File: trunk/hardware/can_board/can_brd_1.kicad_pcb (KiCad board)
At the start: 2 copper layers, 33.5 x 10.9 mm, 9 parts, among them P1 CONN_4, P2 CONN_2, U1 MCP2551

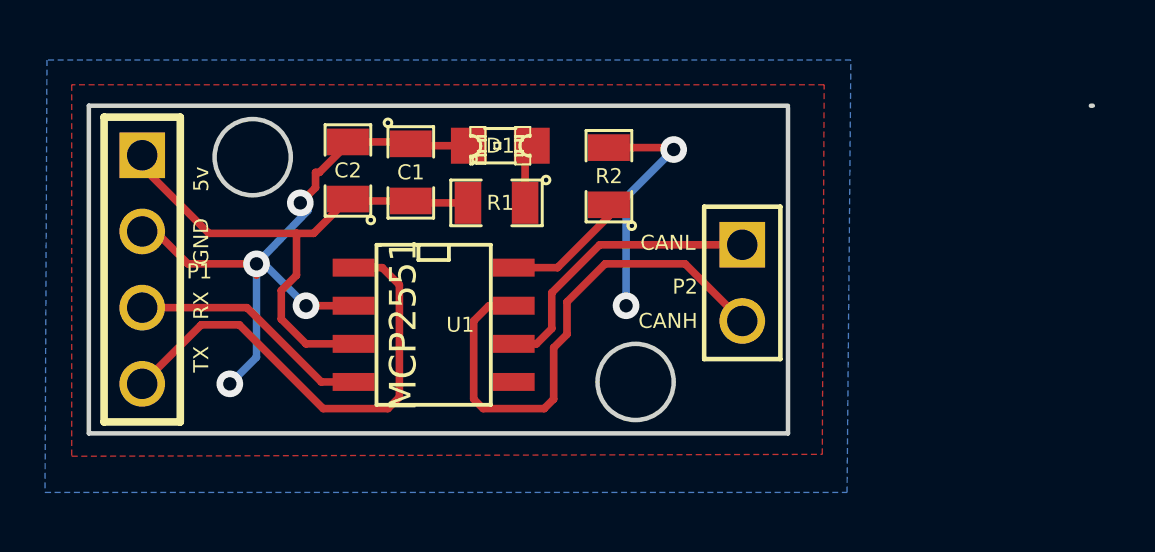
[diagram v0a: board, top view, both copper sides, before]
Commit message: 
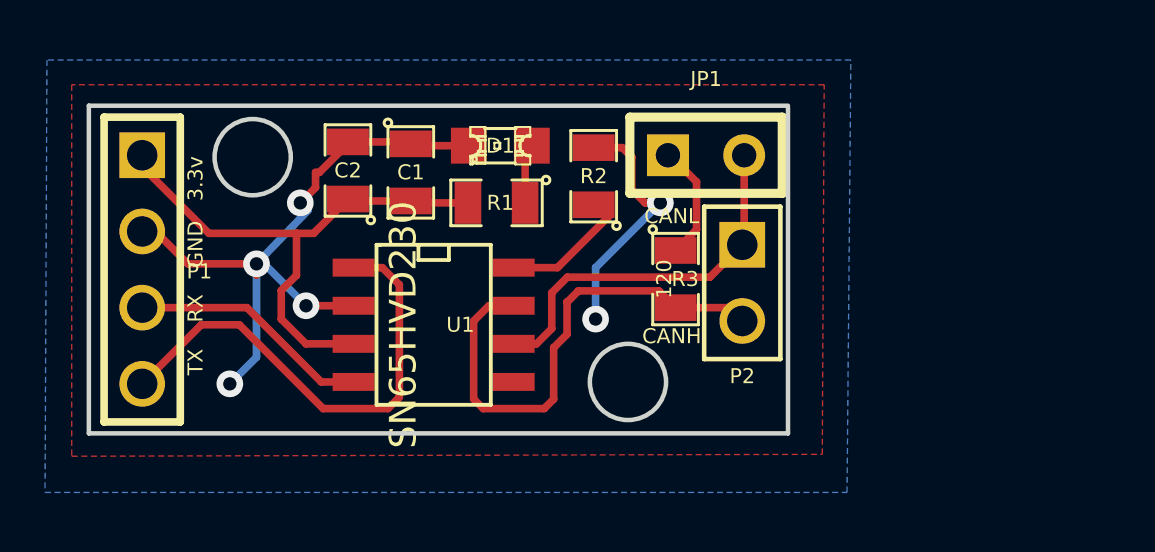
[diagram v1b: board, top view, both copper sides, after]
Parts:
- added JP1: JUMPER, SIL-2, F.Cu at (198.5, 120.6)
- added R3: 120, SM0805, F.Cu at (197.5, 124.7)
- U1: value MCP2551 -> SN65HVD230
- moved R2 0.51 mm to (194.8, 121.3)
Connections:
- net /5V renamed /3.3V
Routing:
- net N-000007: track 0.00 -> 3.90 mm
- net /CANL: track 9.69 -> 12.7 mm
- net /CANH: track 17.7 -> 16.9 mm
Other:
- board size 33.5 x 10.9 mm -> 23.3 x 10.9 mm
- board text added: "TX RX GND 3.3v"
- board text removed: "TX RX GND 5v"

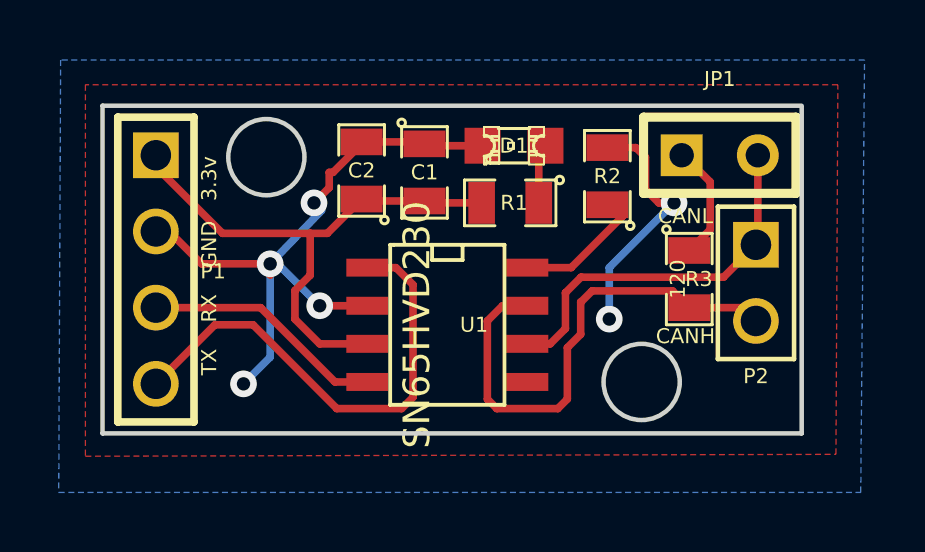
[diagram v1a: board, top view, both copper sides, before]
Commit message: 
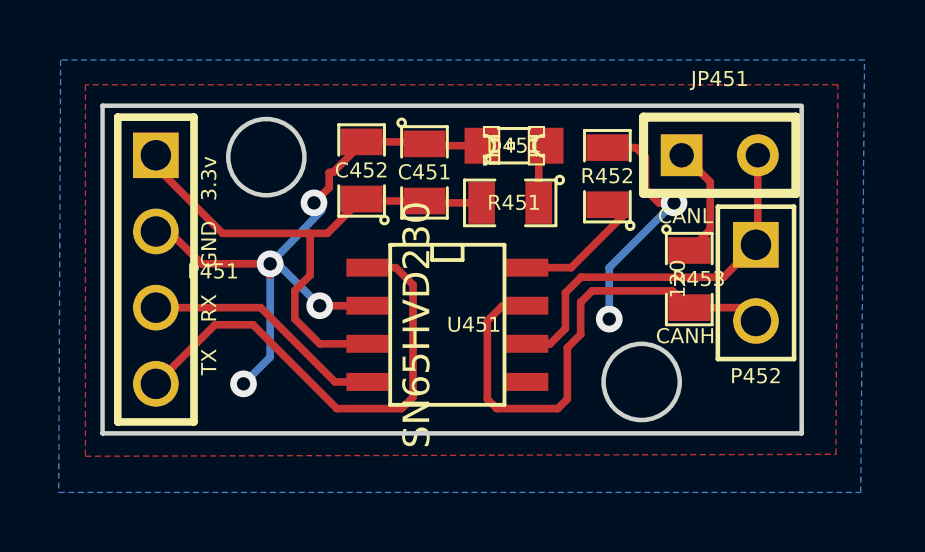
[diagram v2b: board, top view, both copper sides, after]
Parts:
- renumbered C1 to C451, C2 to C452, D1 to D451, G1 to G451, JP1 to JP451, P1 to P451, P2 to P452, R1 to R451, R2 to R452, R3 to R453, U1 to U451
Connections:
- U451 pad 5: N-000009 -> (no net)
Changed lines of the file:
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@@
-(kicad_pcb (version 3) (host pcbnew "(2013-mar-13)-testing")
+(kicad_pcb (version 3) (host pcbnew "(2013-07-07 BZR 4022)-stable")
   (general
     (links 18)
@@
     (zones 0)
     (modules 11)
-    (nets 11)
+    (nets 10)
   )
   (page A4)
   (title_block
-    (date "08 Янв 2014")
     (comment 2 Art_Electro)
     (comment 3 Art_Electro)
@@
   (net 8 N-000007)
   (net 9 N-000008)
-  (net 10 N-000009)
   (net_class Default "Это класс цепей по умолчанию."
     (clearance 0.2032)
@@
     (add_net N-000007)
     (add_net N-000008)
-    (add_net N-000009)
   )
   (module SM0805 (layer F.Cu)
     (at 188.6585 121.158 270)
     (attr smd)
-    (fp_text reference C1 (at 0 0 360) (layer F.SilkS)
+    (fp_text reference C451 (at 0 0 360) (layer F.SilkS)
       (effects (font (size 0.50038 0.50038) (thickness 0.1016)))
     )
@@
     (at 186.563 121.0945 90)
     (attr smd)
-    (fp_text reference C2 (at 0 0 180) (layer F.SilkS)
+    (fp_text reference C452 (at 0 0 180) (layer F.SilkS)
       (effects (font (size 0.50038 0.50038) (thickness 0.1016)))
     )
@@
     (tags "LED 0805 SMD")
     (attr smd)
-    (fp_text reference D1 (at 0 0 360) (layer F.SilkS)
+    (fp_text reference D451 (at 0 0 360) (layer F.SilkS)
       (effects (font (size 0.50038 0.50038) (thickness 0.1016)))
     )
@@
     (at 191.516 122.174 180)
     (attr smd)
-    (fp_text reference R1 (at -0.127 0 360) (layer F.SilkS)
+    (fp_text reference R451 (at -0.127 0 360) (layer F.SilkS)
       (effects (font (size 0.50038 0.50038) (thickness 0.1016)))
     )
@@
     (at 194.7545 121.285 90)
     (attr smd)
-    (fp_text reference R2 (at 0 0 180) (layer F.SilkS)
+    (fp_text reference R452 (at 0 0 180) (layer F.SilkS)
       (effects (font (size 0.50038 0.50038) (thickness 0.1016)))
     )
@@
     (pad 1 smd rect (at -0.9525 0 90) (size 0.889 1.397)
       (layers F.Cu F.Paste F.Mask)
-      (net 9 N-000008)
+      (net 8 N-000007)
     )
     (pad 2 smd rect (at 0.9525 0 90) (size 0.889 1.397)
@@
   (module LOGO_F (layer B.Cu)
     (at 188.976 124.587)
-    (fp_text reference G1 (at 0 -4.14782) (layer B.SilkS) hide
-      (effects (font (thickness 0.3048)) (justify mirror))
+    (fp_text reference G451 (at 0 -4.14782) (layer B.SilkS) hide
+      (effects (font (size 1.524 1.524) (thickness 0.3048)) (justify mirror))
     )
     (fp_text value LOGO (at 0 4.14782) (layer B.SilkS) hide
-      (effects (font (thickness 0.3048)) (justify mirror))
+      (effects (font (size 1.524 1.524) (thickness 0.3048)) (justify mirror))
     )
     (fp_poly (pts (xy 3.34518 -0.04318) (xy 3.3401 0.381) (xy 3.32486 0.68326) (xy 3.28676 0.90932)
@@
     (descr "Double rangee de contacts 2 x 5 pins")
     (tags CONN)
-    (fp_text reference P1 (at 0.0635 -1.905 360) (layer F.SilkS)
+    (fp_text reference P451 (at 0.0635 -1.905 360) (layer F.SilkS)
       (effects (font (size 0.50038 0.50038) (thickness 0.1016)))
     )
@@
     (descr "Connecter 2 pins")
     (tags "PIN 2")
-    (fp_text reference P2 (at 3.1115 0 360) (layer F.SilkS)
+    (fp_text reference P452 (at 3.1115 0 360) (layer F.SilkS)
       (effects (font (size 0.50038 0.50038) (thickness 0.1016)))
     )
@@
     (tags "CMS SOJ")
     (attr smd)
-    (fp_text reference U1 (at 0 -0.889 360) (layer F.SilkS)
+    (fp_text reference U451 (at 0 -0.889 360) (layer F.SilkS)
       (effects (font (size 0.50038 0.50038) (thickness 0.1016)))
     )
@@
     (pad 8 smd rect (at -1.905 -2.667 270) (size 0.59944 1.39954)
       (layers F.Cu F.Paste F.Mask)
-      (net 9 N-000008)
+      (net 8 N-000007)
     )
     (pad 1 smd rect (at -1.905 2.667 270) (size 0.59944 1.39954)
@@
     (pad 5 smd rect (at 1.905 -2.667 270) (size 0.59944 1.39954)
       (layers F.Cu F.Paste F.Mask)
-      (net 10 N-000009)
     )
     (pad 2 smd rect (at -0.635 2.667 270) (size 0.59944 1.39954)
@@
     (descr "Connecteurs 2 pins")
     (tags "CONN DEV")
-    (fp_text reference JP1 (at 0 -2.54) (layer F.SilkS)
+    (fp_text reference JP451 (at 0 -2.54) (layer F.SilkS)
       (effects (font (size 0.50038 0.50038) (thickness 0.1016)))
     )
@@
     (pad 1 thru_hole rect (at -1.27 0) (size 1.397 1.397) (drill 0.8128)
       (layers *.Cu *.Mask F.SilkS)
-      (net 8 N-000007)
+      (net 9 N-000008)
     )
     (pad 2 thru_hole circle (at 1.27 0) (size 1.397 1.397) (drill 0.8128)
@@
     (at 197.485 124.714 270)
     (attr smd)
-    (fp_text reference R3 (at 0 -0.3175 360) (layer F.SilkS)
+    (fp_text reference R453 (at 0 -0.3175 360) (layer F.SilkS)
       (effects (font (size 0.50038 0.50038) (thickness 0.10922)))
     )
@@
     (pad 1 smd rect (at -0.9525 0 270) (size 0.889 1.397)
       (layers F.Cu F.Paste F.Mask)
-      (net 8 N-000007)
+      (net 9 N-000008)
     )
     (pad 2 smd rect (at 0.9525 0 270) (size 0.889 1.397)
@@
   (segment (start 192.4685 122.174) (end 192.4685 120.49252) (width 0.254) (layer F.Cu) (net 7))
   (segment (start 192.4685 120.49252) (end 192.69202 120.269) (width 0.254) (layer F.Cu) (net 7))
-  (segment (start 197.231 120.5865) (end 197.2945 120.5865) (width 0.254) (layer F.Cu) (net 8))
-  (segment (start 198.1835 123.063) (end 197.485 123.7615) (width 0.254) (layer F.Cu) (net 8))
-  (segment (start 198.1835 121.4755) (end 198.1835 123.063) (width 0.254) (layer F.Cu) (net 8))
-  (segment (start 197.2945 120.5865) (end 198.1835 121.4755) (width 0.254) (layer F.Cu) (net 8))
-  (segment (start 192.0875 124.333) (end 193.548 124.333) (width 0.254) (layer F.Cu) (net 9))
-  (segment (start 195.2625 122.6185) (end 195.2625 122.2375) (width 0.254) (layer F.Cu) (net 9))
-  (segment (start 193.548 124.333) (end 195.2625 122.6185) (width 0.254) (layer F.Cu) (net 9))
-  (segment (start 194.7545 122.301) (end 194.691 122.301) (width 0.254) (layer F.Cu) (net 9) (status 80000))
+  (segment (start 192.0875 124.333) (end 193.548 124.333) (width 0.254) (layer F.Cu) (net 8))
+  (segment (start 195.2625 122.6185) (end 195.2625 122.2375) (width 0.254) (layer F.Cu) (net 8))
+  (segment (start 193.548 124.333) (end 195.2625 122.6185) (width 0.254) (layer F.Cu) (net 8))
+  (segment (start 194.7545 122.301) (end 194.691 122.301) (width 0.254) (layer F.Cu) (net 8) (status 80000))
+  (segment (start 197.231 120.5865) (end 197.2945 120.5865) (width 0.254) (layer F.Cu) (net 9))
+  (segment (start 198.1835 123.063) (end 197.485 123.7615) (width 0.254) (layer F.Cu) (net 9))
+  (segment (start 198.1835 121.4755) (end 198.1835 123.063) (width 0.254) (layer F.Cu) (net 9))
+  (segment (start 197.2945 120.5865) (end 198.1835 121.4755) (width 0.254) (layer F.Cu) (net 9))
   (zone (net 6) (net_name GND) (layer F.Cu) (hatch edge 0.508)
     (connect_pads (clearance 0.3))

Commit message: new location
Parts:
- moved C451 73.1 mm to (145.5, 180.1)
- moved C452 73.1 mm to (143.4, 180.0)
- moved P452 73.1 mm to (156.5, 183.8)
- moved D451 73.1 mm to (148.5, 179.2)
- moved G451 73.1 mm to (145.8, 183.5)
- moved JP451 73.1 mm to (155.3, 179.5)
- moved P451 73.1 mm to (136.5, 183.3)
- moved R452 73.1 mm to (151.6, 180.2)
- moved R453 73.1 mm to (154.3, 183.6)
- moved U451 73.1 mm to (146.2, 185.2)
- moved R451 73.1 mm to (148.3, 181.1)
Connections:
- net /RX renamed /CAN_RX
- net /TX renamed /CAN_TX

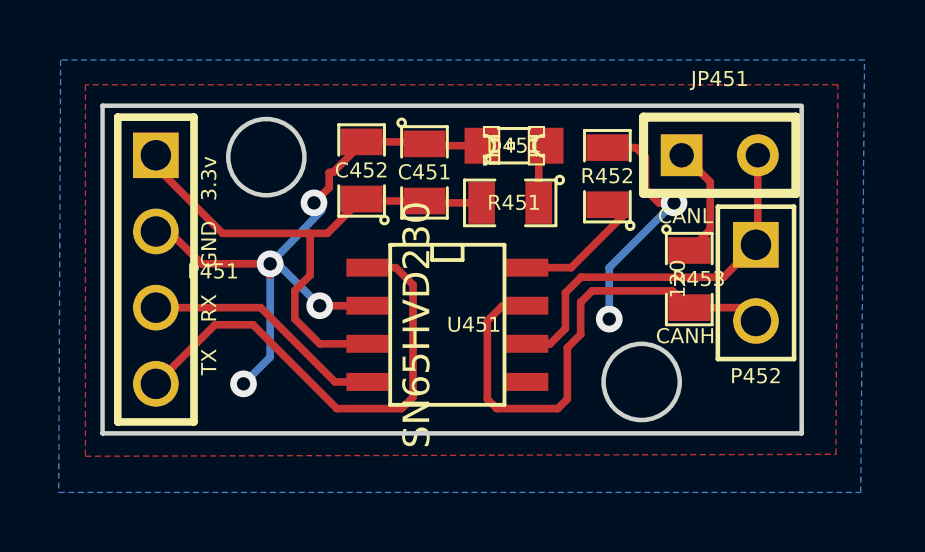
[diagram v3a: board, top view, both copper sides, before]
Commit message: name range fix
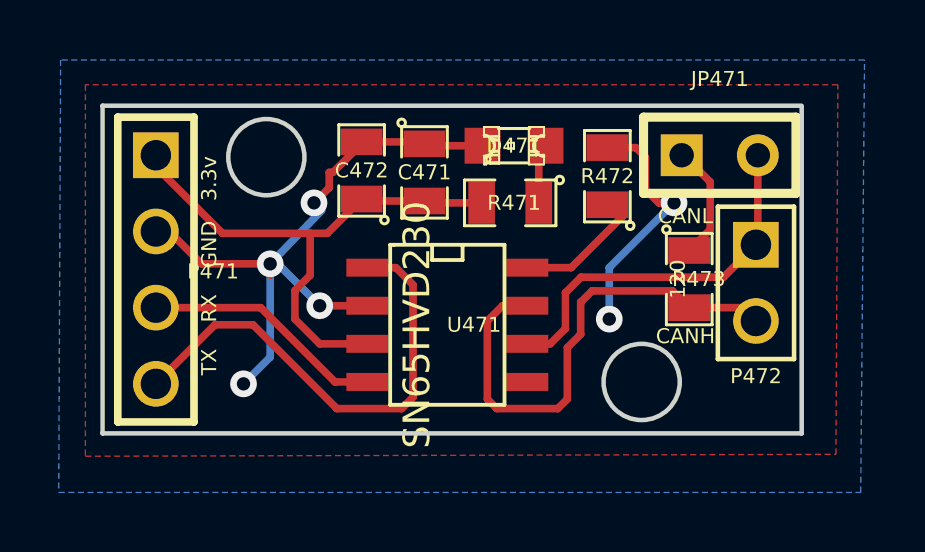
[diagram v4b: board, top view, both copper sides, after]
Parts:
- renumbered C451 to C471, C452 to C472, D451 to D471, G451 to G471, JP451 to JP471, P451 to P471, P452 to P472, R451 to R471, R452 to R472, R453 to R473, U451 to U471
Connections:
- net /CAN_RX renamed /RX
- net /CAN_TX renamed /TX
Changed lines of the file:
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@@
   (net 2 /CANH)
   (net 3 /CANL)
-  (net 4 /CAN_RX)
-  (net 5 /CAN_TX)
+  (net 4 /RX)
+  (net 5 /TX)
   (net 6 GND)
   (net 7 N-0000010)
@@
     (add_net /CANH)
     (add_net /CANL)
-    (add_net /CAN_RX)
-    (add_net /CAN_TX)
+    (add_net /RX)
+    (add_net /TX)
     (add_net GND)
     (add_net N-0000010)
@@
     (at 145.4785 180.086 270)
     (attr smd)
-    (fp_text reference C451 (at 0 0 360) (layer F.SilkS)
+    (fp_text reference C471 (at 0 0 360) (layer F.SilkS)
       (effects (font (size 0.50038 0.50038) (thickness 0.1016)))
     )
@@
     (at 143.383 180.0225 90)
     (attr smd)
-    (fp_text reference C452 (at 0 0 180) (layer F.SilkS)
+    (fp_text reference C472 (at 0 0 180) (layer F.SilkS)
       (effects (font (size 0.50038 0.50038) (thickness 0.1016)))
     )
@@
     (tags "LED 0805 SMD")
     (attr smd)
-    (fp_text reference D451 (at 0 0 360) (layer F.SilkS)
+    (fp_text reference D471 (at 0 0 360) (layer F.SilkS)
       (effects (font (size 0.50038 0.50038) (thickness 0.1016)))
     )
@@
     (at 148.336 181.102 180)
     (attr smd)
-    (fp_text reference R451 (at -0.127 0 360) (layer F.SilkS)
+    (fp_text reference R471 (at -0.127 0 360) (layer F.SilkS)
       (effects (font (size 0.50038 0.50038) (thickness 0.1016)))
     )
@@
     (at 151.5745 180.213 90)
     (attr smd)
-    (fp_text reference R452 (at 0 0 180) (layer F.SilkS)
+    (fp_text reference R472 (at 0 0 180) (layer F.SilkS)
       (effects (font (size 0.50038 0.50038) (thickness 0.1016)))
     )
@@
   (module LOGO_F (layer B.Cu)
     (at 145.796 183.515)
-    (fp_text reference G451 (at 0 -4.14782) (layer B.SilkS) hide
+    (fp_text reference G471 (at 0 -4.14782) (layer B.SilkS) hide
       (effects (font (size 1.524 1.524) (thickness 0.3048)) (justify mirror))
     )
@@
     (descr "Double rangee de contacts 2 x 5 pins")
     (tags CONN)
-    (fp_text reference P451 (at 0.0635 -1.905 360) (layer F.SilkS)
+    (fp_text reference P471 (at 0.0635 -1.905 360) (layer F.SilkS)
       (effects (font (size 0.50038 0.50038) (thickness 0.1016)))
     )
@@
     (pad 3 thru_hole circle (at 1.27 0 270) (size 1.524 1.524) (drill 1.016)
       (layers *.Cu *.Mask F.SilkS)
-      (net 4 /CAN_RX)
+      (net 4 /RX)
     )
     (pad 4 thru_hole circle (at 3.81 0 270) (size 1.524 1.524) (drill 1.016)
       (layers *.Cu *.Mask F.SilkS)
-      (net 5 /CAN_TX)
+      (net 5 /TX)
     )
     (model pin_array\pins_array_4x1.wrl
@@
     (descr "Connecter 2 pins")
     (tags "PIN 2")
-    (fp_text reference P452 (at 3.1115 0 360) (layer F.SilkS)
+    (fp_text reference P472 (at 3.1115 0 360) (layer F.SilkS)
       (effects (font (size 0.50038 0.50038) (thickness 0.1016)))
     )
@@
     (tags "CMS SOJ")
     (attr smd)
-    (fp_text reference U451 (at 0 -0.889 360) (layer F.SilkS)
+    (fp_text reference U471 (at 0 -0.889 360) (layer F.SilkS)
       (effects (font (size 0.50038 0.50038) (thickness 0.1016)))
     )
@@
     (pad 1 smd rect (at -1.905 2.667 270) (size 0.59944 1.39954)
       (layers F.Cu F.Paste F.Mask)
-      (net 5 /CAN_TX)
+      (net 5 /TX)
     )
     (pad 7 smd rect (at -0.635 -2.667 270) (size 0.59944 1.39954)
@@
     (pad 4 smd rect (at 1.905 2.667 270) (size 0.59944 1.39954)
       (layers F.Cu F.Paste F.Mask)
-      (net 4 /CAN_RX)
+      (net 4 /RX)
     )
     (model smd/cms_so8.wrl
@@
     (descr "Connecteurs 2 pins")
     (tags "CONN DEV")
-    (fp_text reference JP451 (at 0 -2.54) (layer F.SilkS)
+    (fp_text reference JP471 (at 0 -2.54) (layer F.SilkS)
       (effects (font (size 0.50038 0.50038) (thickness 0.1016)))
     )
@@
     (at 154.305 183.642 270)
     (attr smd)
-    (fp_text reference R453 (at 0 -0.3175 360) (layer F.SilkS)
+    (fp_text reference R473 (at 0 -0.3175 360) (layer F.SilkS)
       (effects (font (size 0.50038 0.50038) (thickness 0.10922)))
     )

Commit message: better net names
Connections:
- net /RX renamed /CAN_RX
- net /TX renamed /CAN_TX
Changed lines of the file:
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@@
   (net 2 /CANH)
   (net 3 /CANL)
-  (net 4 /RX)
-  (net 5 /TX)
+  (net 4 /CAN_RX)
+  (net 5 /CAN_TX)
   (net 6 GND)
   (net 7 N-0000010)
@@
     (add_net /CANH)
     (add_net /CANL)
-    (add_net /RX)
-    (add_net /TX)
+    (add_net /CAN_RX)
+    (add_net /CAN_TX)
     (add_net GND)
     (add_net N-0000010)
@@
     (pad 3 thru_hole circle (at 1.27 0 270) (size 1.524 1.524) (drill 1.016)
       (layers *.Cu *.Mask F.SilkS)
-      (net 4 /RX)
+      (net 4 /CAN_RX)
     )
     (pad 4 thru_hole circle (at 3.81 0 270) (size 1.524 1.524) (drill 1.016)
       (layers *.Cu *.Mask F.SilkS)
-      (net 5 /TX)
+      (net 5 /CAN_TX)
     )
     (model pin_array\pins_array_4x1.wrl
@@
     (pad 1 smd rect (at -1.905 2.667 270) (size 0.59944 1.39954)
       (layers F.Cu F.Paste F.Mask)
-      (net 5 /TX)
+      (net 5 /CAN_TX)
     )
     (pad 7 smd rect (at -0.635 -2.667 270) (size 0.59944 1.39954)
@@
     (pad 4 smd rect (at 1.905 2.667 270) (size 0.59944 1.39954)
       (layers F.Cu F.Paste F.Mask)
-      (net 4 /RX)
+      (net 4 /CAN_RX)
     )
     (model smd/cms_so8.wrl
